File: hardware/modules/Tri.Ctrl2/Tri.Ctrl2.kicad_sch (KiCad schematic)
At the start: 0 parts

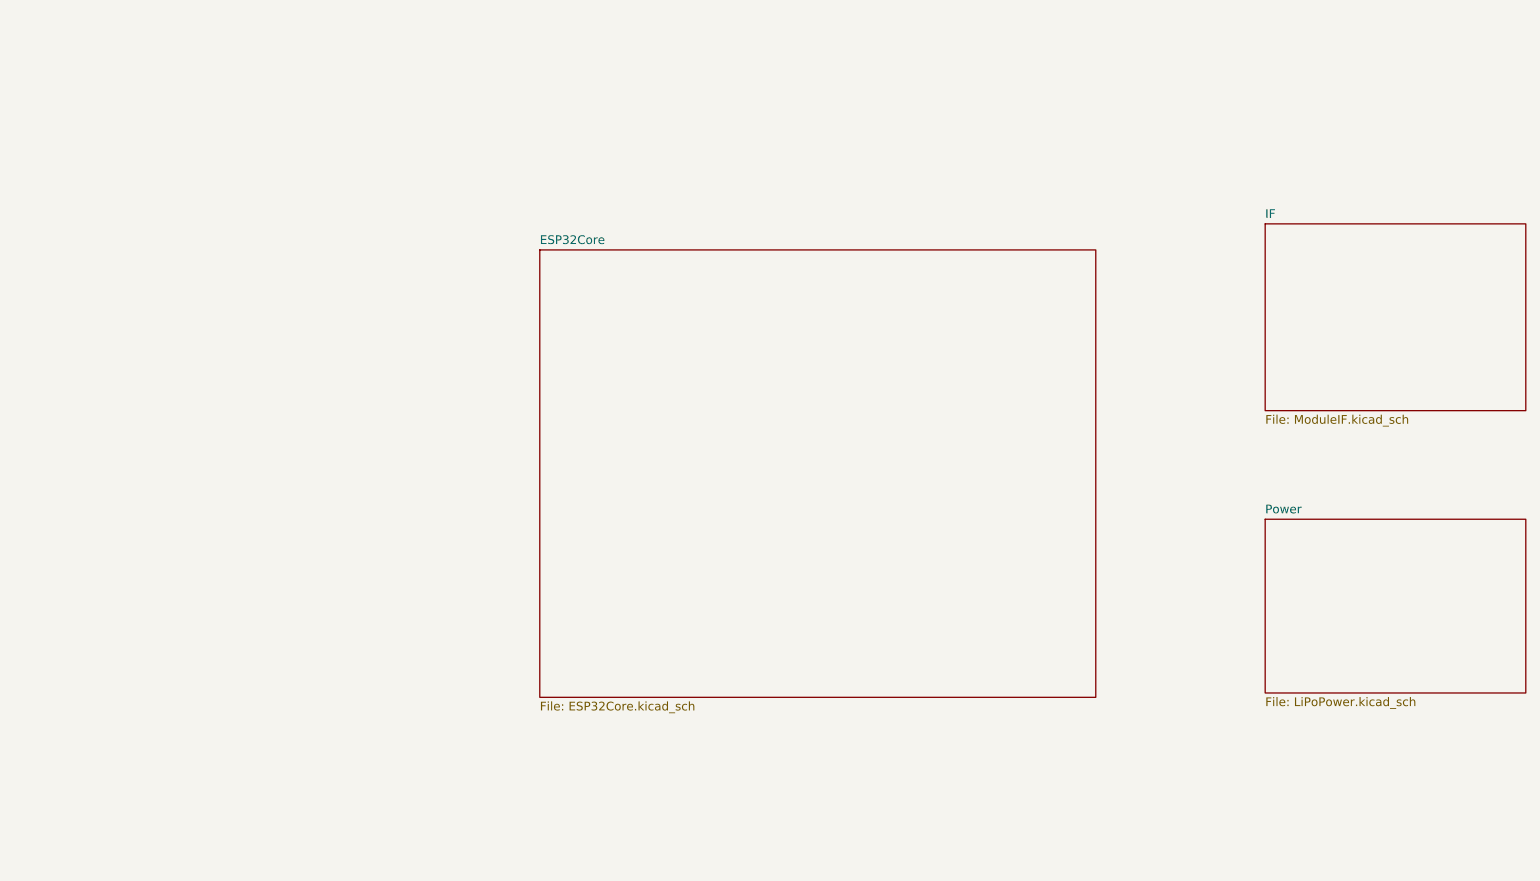
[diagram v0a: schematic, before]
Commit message: ICSコンポーネント製作
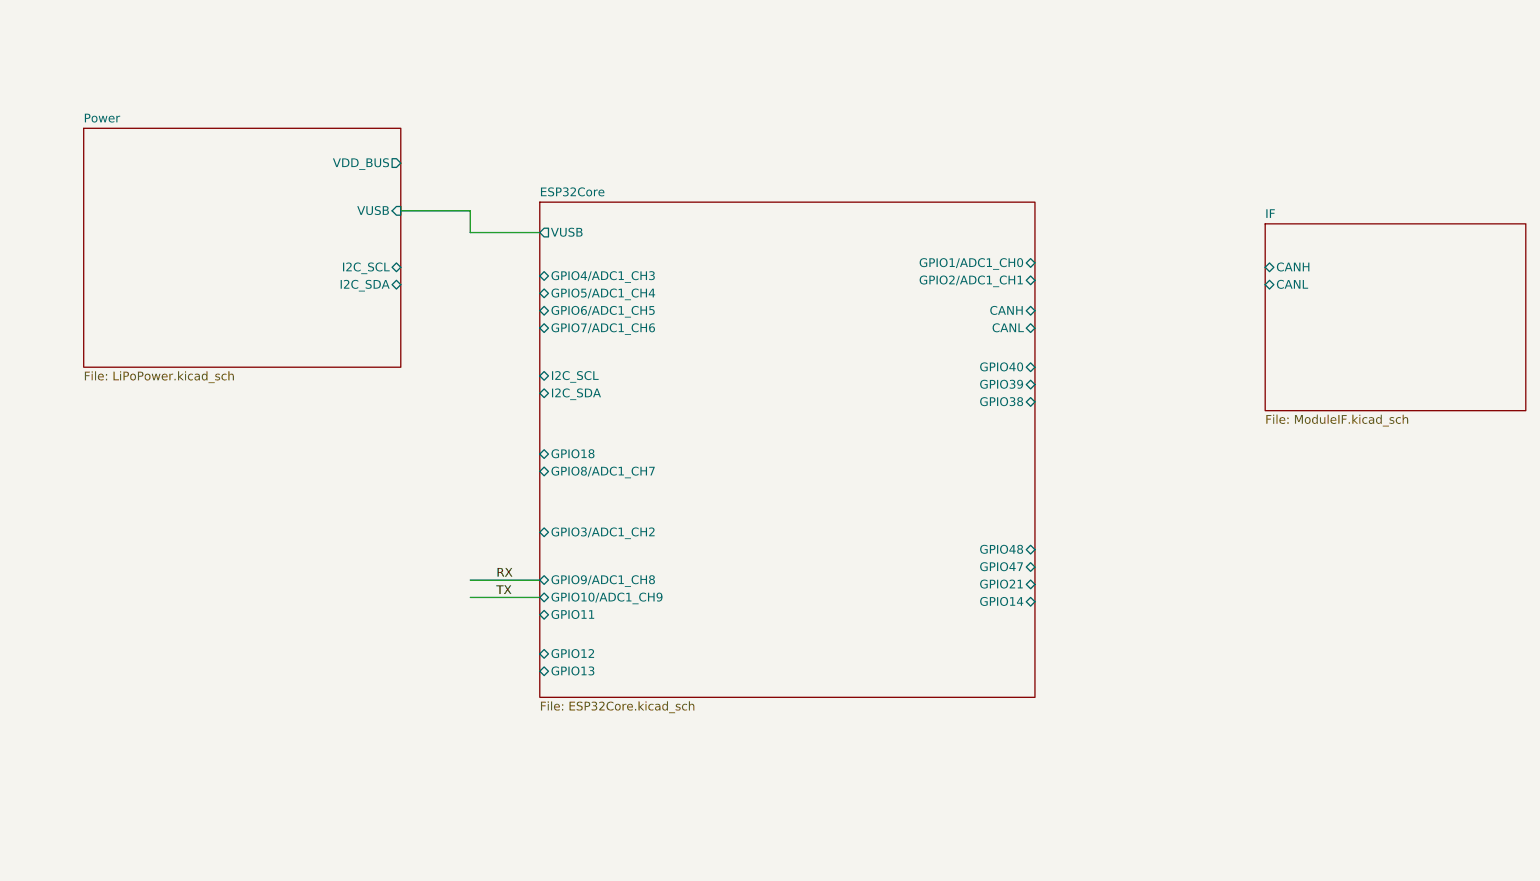
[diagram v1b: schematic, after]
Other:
- sheet ESP32Core ports: added CANH, CANL, GPIO10/ADC1_CH9, GPIO11, GPIO12, GPIO13, GPIO14, GPIO18, GPIO1/ADC1_CH0, GPIO21, GPIO2/ADC1_CH1, GPIO38, GPIO39, GPIO3/ADC1_CH2, GPIO40, GPIO47, GPIO48, GPIO4/ADC1_CH3, GPIO5/ADC1_CH4, GPIO6/ADC1_CH5, GPIO7/ADC1_CH6, GPIO8/ADC1_CH7, GPIO9/ADC1_CH8, I2C_SCL, I2C_SDA, VUSB; removed none
- sheet IF ports: added CANH, CANL; removed none
- sheet Power ports: added I2C_SCL, I2C_SDA, VDD_BUS, VUSB; removed none

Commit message: 回路図ひととおり完了
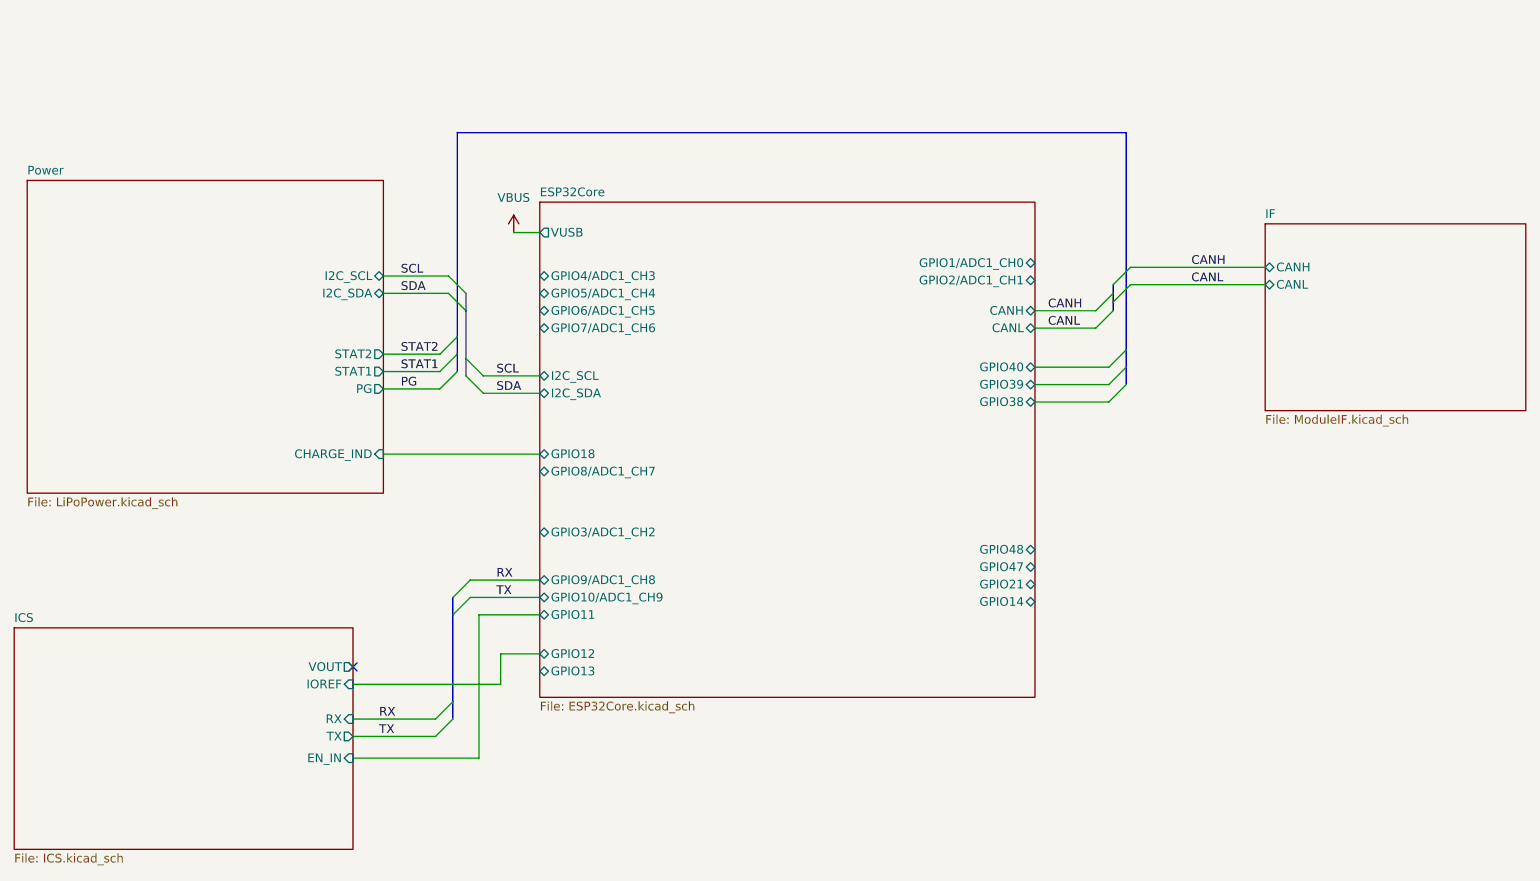
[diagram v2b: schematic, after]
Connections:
- no-connect marks 0 -> 1
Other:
- added sheet ICS (ICS.kicad_sch)
- sheet Power ports: added CHARGE_IND, PG, STAT1, STAT2; removed VDD_BUS, VUSB

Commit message: ひととおり配置
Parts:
- added B101: ~, WOBCLibrary:Board_1U_60x60, symbol WOBCLibrary:Board
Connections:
- new net GND: B101.GND
- no-connect marks 1 -> 13
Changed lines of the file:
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@@
 	(paper "A4")
 	(no_connect
+		(at 173.99 70.485)
+	)
+	(no_connect
+		(at 101.6 130.175)
+	)
+	(no_connect
+		(at 173.99 114.935)
+	)
+	(no_connect
+		(at 173.99 120.015)
+	)
+	(no_connect
+		(at 101.6 80.01)
+	)
+	(no_connect
+		(at 173.99 112.395)
+	)
+	(no_connect
+		(at 101.6 77.47)
+	)
+	(no_connect
 		(at 74.295 129.54)
+	)
+	(no_connect
+		(at 173.99 117.475)
+	)
+	(no_connect
+		(at 101.6 100.965)
+	)
+	(no_connect
+		(at 101.6 74.93)
+	)
+	(no_connect
+		(at 101.6 72.39)
+	)
+	(no_connect
+		(at 173.99 73.025)
 	)
 	(bus_entry
@@
 		)
 	)
+	(label "STAT2"
+		(at 175.895 88.265 0)
+		(fields_autoplaced yes)
+		(effects
+			(font
+				(size 1.27 1.27)
+			)
+			(justify left bottom)
+		)
+	)
 	(label "RX"
 		(at 95.25 116.84 0)
@@
 	(label "TX"
 		(at 78.105 139.7 0)
+		(fields_autoplaced yes)
+		(effects
+			(font
+				(size 1.27 1.27)
+			)
+			(justify left bottom)
+		)
+	)
+	(label "STAT1"
+		(at 175.895 90.805 0)
+		(fields_autoplaced yes)
+		(effects
+			(font
+				(size 1.27 1.27)
+			)
+			(justify left bottom)
+		)
+	)
+	(label "PG"
+		(at 175.895 85.725 0)
 		(fields_autoplaced yes)
 		(effects
@@
 		(dnp no)
 		(fields_autoplaced yes)
-		(property "Reference" "#PWR0102"
+		(property "Reference" "#PWR0101"
 			(at 97.79 69.85 0)
 			(effects
@@
 			(project ""
 				(path "/80fbddc6-aa50-4ba3-b7b9-21fad44f05f1"
-					(reference "#PWR0102")
+					(reference "#PWR0101")
 					(unit 1)
 				)
+			)
+		)
+	)
+	(symbol
+		(lib_id "WOBCLibrary:Board")
+		(at 139.065 34.925 0)
+		(unit 1)
+		(exclude_from_sim no)
+		(in_bom yes)
+		(on_board yes)
+		(dnp no)
+		(fields_autoplaced yes)
+		(property "Reference" "B101"
+			(at 140.97 35.3567 0)
+			(effects
+				(font
+					(size 1.27 1.27)
+				)
+				(justify left)
+			)
+		)
+		(property "Value" "~"
+			(at 140.97 37.2618 0)
+			(effects
+				(font
+					(size 1.27 1.27)
+				)
+				(justify left)
+			)
+		)
+		(property "Footprint" "WOBCLibrary:Board_1U_60x60"
+			(at 139.065 34.925 0)
+			(effects
+				(font
+					(size 1.27 1.27)
+				)
+				(hide yes)
+			)
+		)
+		(property "Datasheet" ""
+			(at 139.065 34.925 0)
+			(effects
+				(font
+					(size 1.27 1.27)
+				)
+				(hide yes)
+			)
+		)
+		(property "Description" ""
+			(at 139.065 34.925 0)
+			(effects
+				(font
+					(size 1.27 1.27)
+				)
+				(hide yes)
+			)
+		)
+		(pin "GND"
+		)
+		(instances
+			(project ""
+				(path "/80fbddc6-aa50-4ba3-b7b9-21fad44f05f1"
+					(reference "B101")
+					(unit 1)
+				)

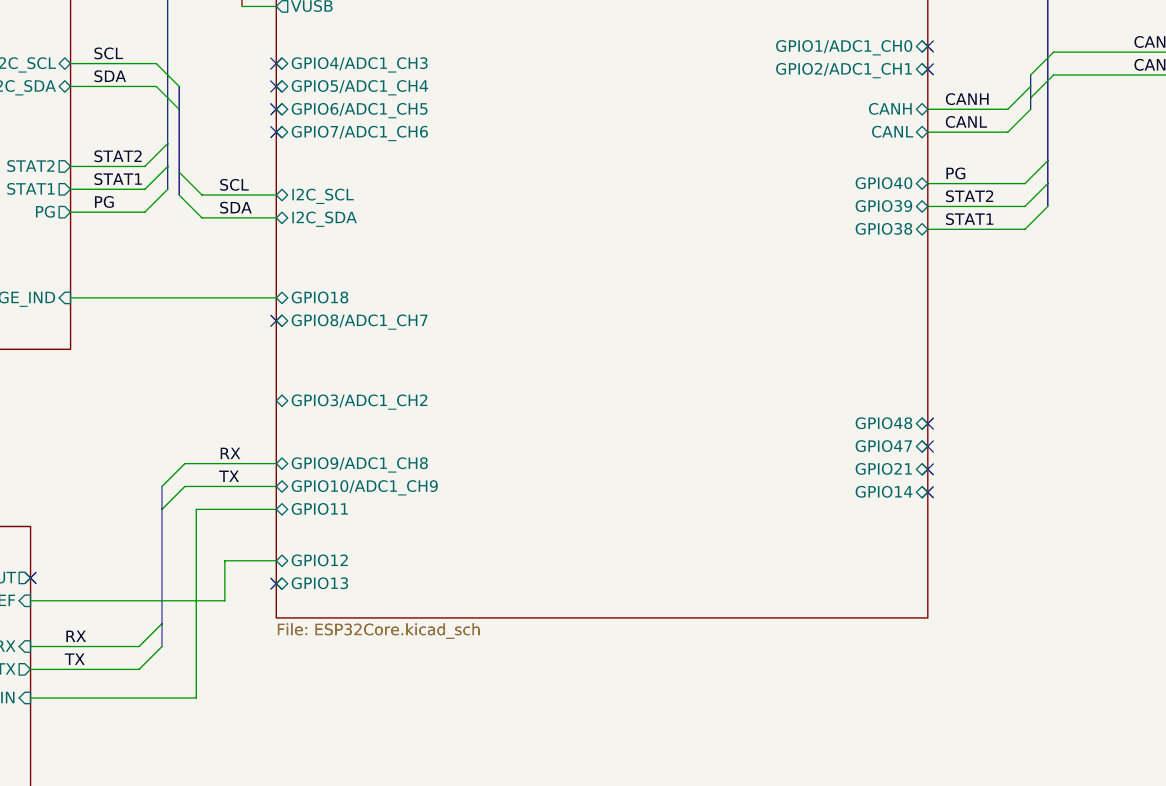
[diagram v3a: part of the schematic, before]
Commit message: ひととおり配線
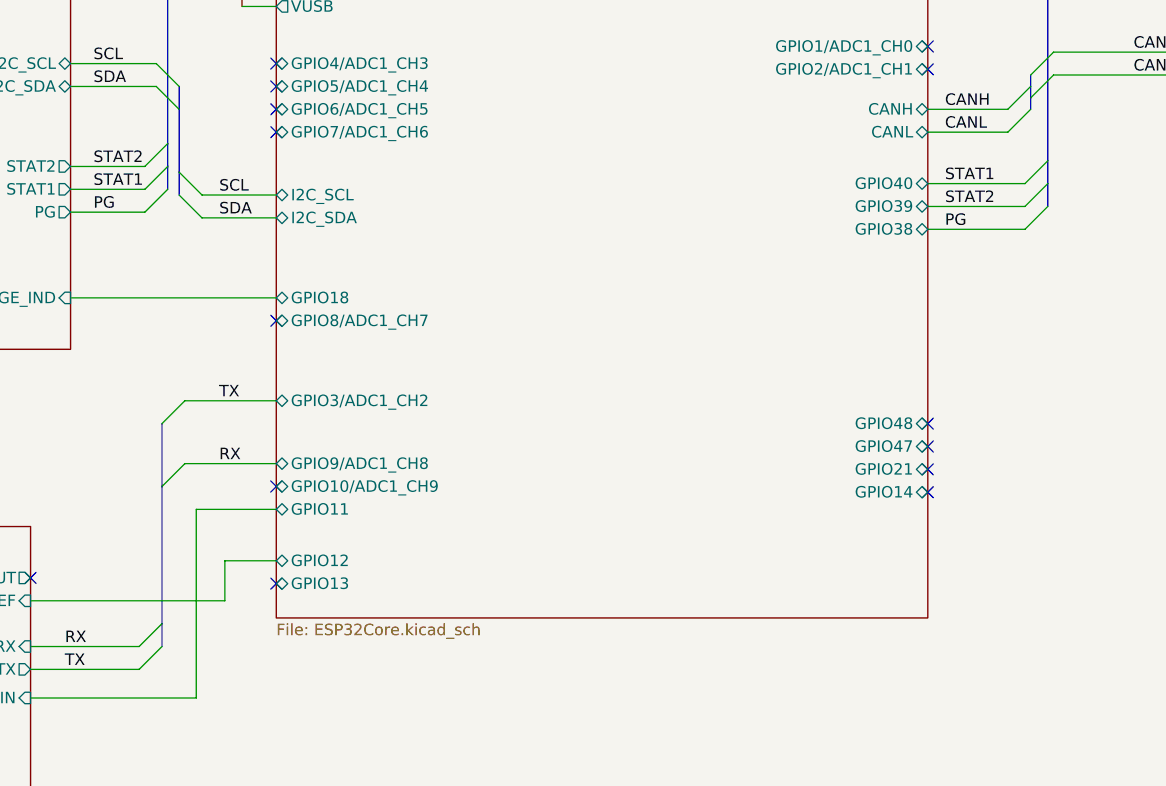
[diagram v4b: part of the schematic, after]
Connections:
- no-connect marks 13 -> 14
